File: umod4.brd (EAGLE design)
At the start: 104.9 x 71.1 mm, 94 parts, among them IC3 27C256-FEED-THRU, J1 DMSAT-SF-PEJ, J2 10118194-0001LF, J4 CORTEX_DEBUG-PTH, J5 JST BM08B-SRSS, M1 RPi Pico W, M2 Generic single-sided NEO-8, Q1 C10487/SI2301CDS, Q2 SS8050, U1 74LVC541, U2 74LVC4245, U3 74LVC541, U4 RP2040, U5 W25Q128JVSIQ, U6 74LVC2G04, U7 74LVC2G04, U8 WS2812C-2020, U9 LGS5148, Y1 12MHz

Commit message: Latest changes after github token changed
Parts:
- removed TP2: (no value), SparkFun-Connectors:PAD.03X.05
- added C34: N/S, robins-v7:SMD-0603
- moved JP2 1.78 mm to (34.5, 38.9)
- moved R13 0.76 mm to (58.2, 34.5)
- moved S1 0.51 mm to (63.2, 35.3)
- moved R19 0.25 mm to (8.38, 47.8)
- moved R9 0.25 mm to (8.38, 46.2)
- moved C13 0.25 mm to (24.1, 29.5)
- moved C14 0.25 mm to (24.1, 35.8)
- moved C27 0.25 mm to (24.1, 34.0)
- moved R14 0.25 mm to (24.1, 38.1)
- moved R15 0.25 mm to (24.1, 31.2)
- moved R16 0.25 mm to (24.1, 40.4)
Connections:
- new net SPARE1: M1.31
- net N$16: now also C34.P$2
- net VSYS_1: now also C34.P$1
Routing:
- net +12_US: track 18.3 -> 36.6 mm
- net +3V3: track 336.5 -> 330.9 mm
- net VSYS_1: track 29.7 -> 34.3 mm
- net VIN_MEAS: track 59.4 -> 55.9 mm
- net SPARE1: track 0.00 -> 3.32 mm, vias 0 -> 1
- net SPARE0: track 0.00 -> 3.32 mm, vias 0 -> 1
- net N$16: track 3.98 -> 5.28 mm
- net EP_RUN: track 97.9 -> 96.9 mm
- net N$7: track 36.0 -> 35.1 mm
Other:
- outline, holes or cut-outs redrawn
- board text added: "SP0"
- board text added: "SP1"

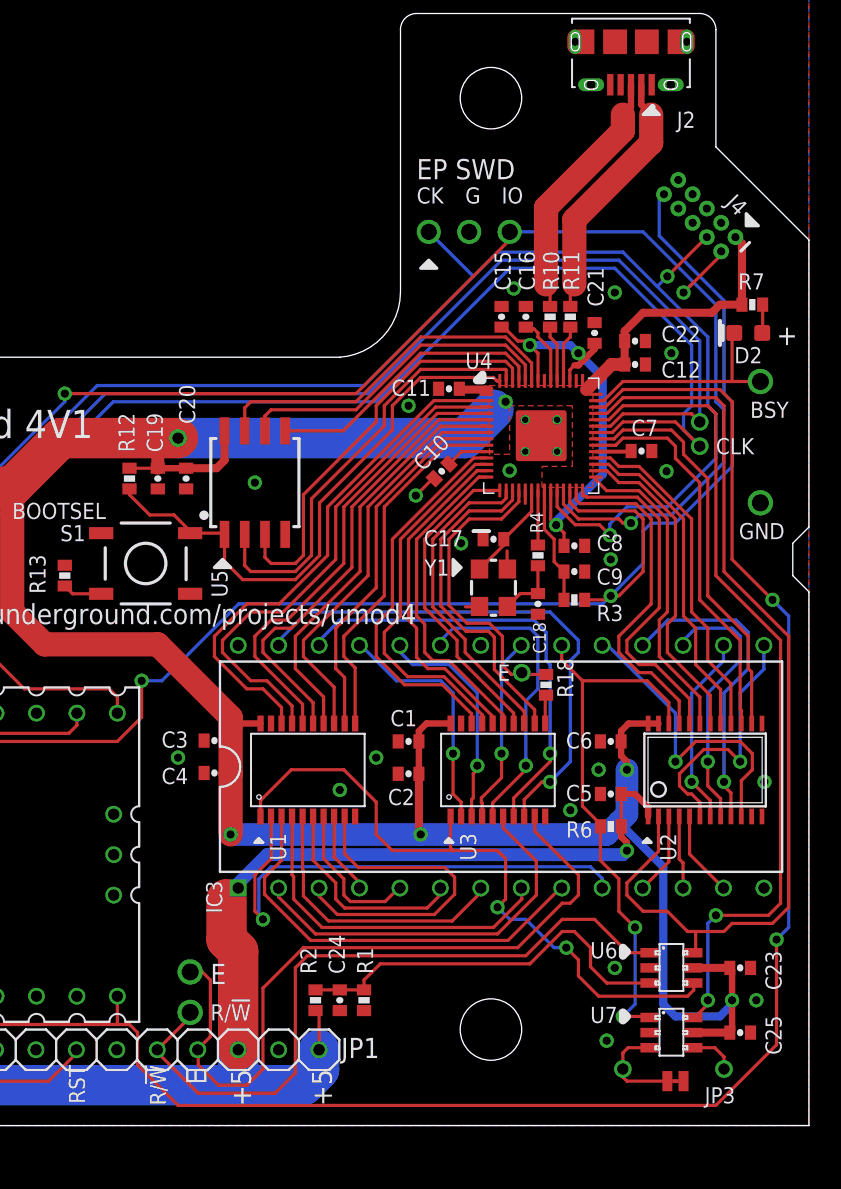
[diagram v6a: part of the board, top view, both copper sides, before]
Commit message: Updated debugger connections for WP, EP
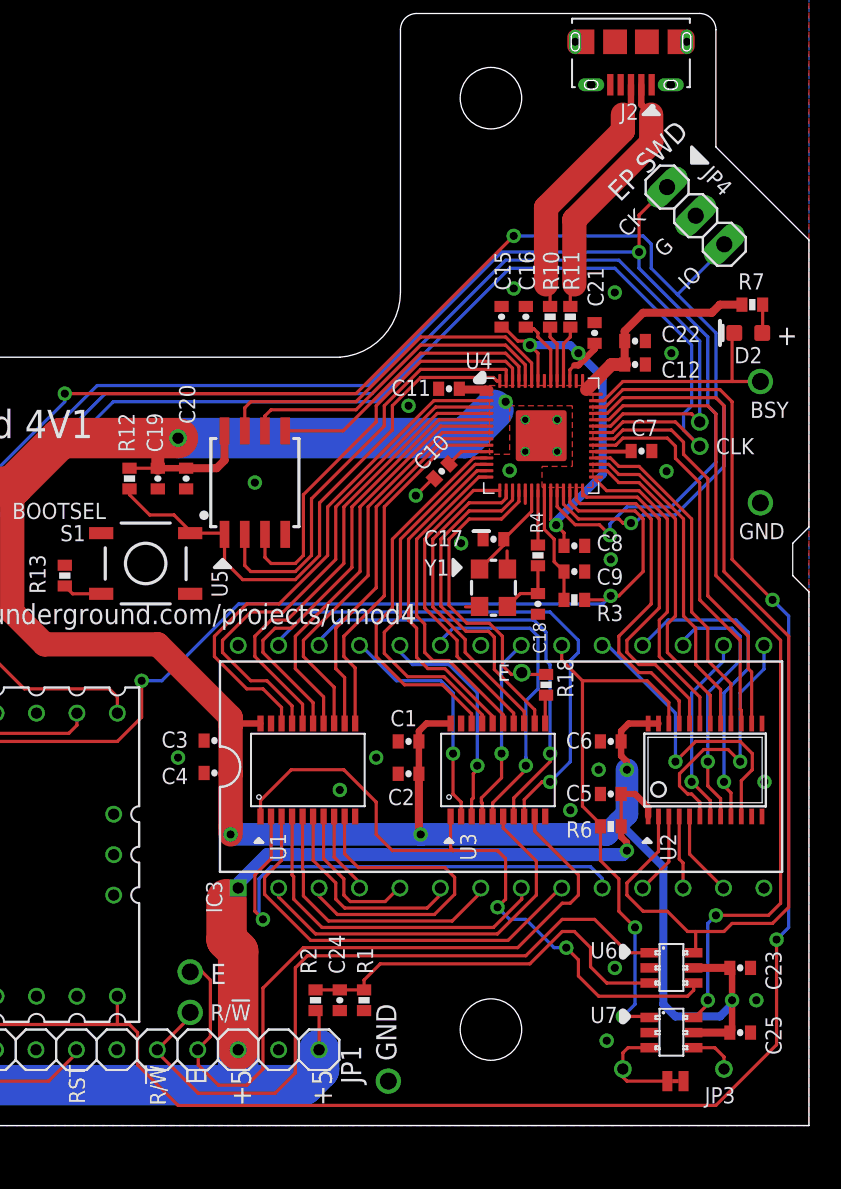
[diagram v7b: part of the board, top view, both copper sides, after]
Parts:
- removed J4: CORTEX_DEBUG-PTH, robins-v7:CON-2X5-1.27MM
- added JP4: (no value), pinhead:1X03
- added TP2: (no value), robins-v7:KEYSTONE-1035
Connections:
- net +3V3: no longer J4.1
- net EP_RUN: no longer J4.10
- net GND: now also JP4.2, TP2.P$1; no longer J4.3, J4.5, J4.9
- net RP_SWCLK: now also JP4.1; no longer J4.4
- net RP_SWD: now also JP4.3; no longer J4.2
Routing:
- net EP_RUN: track 96.9 -> 65.6 mm
- net +3V3: track 330.9 -> 326.5 mm
- net RP_SWCLK: track 137.7 -> 134.9 mm, vias 4 -> 3
- net RP_SWD: track 136.8 -> 136.3 mm, vias 5 -> 4
- net GND: vias 30 -> 29

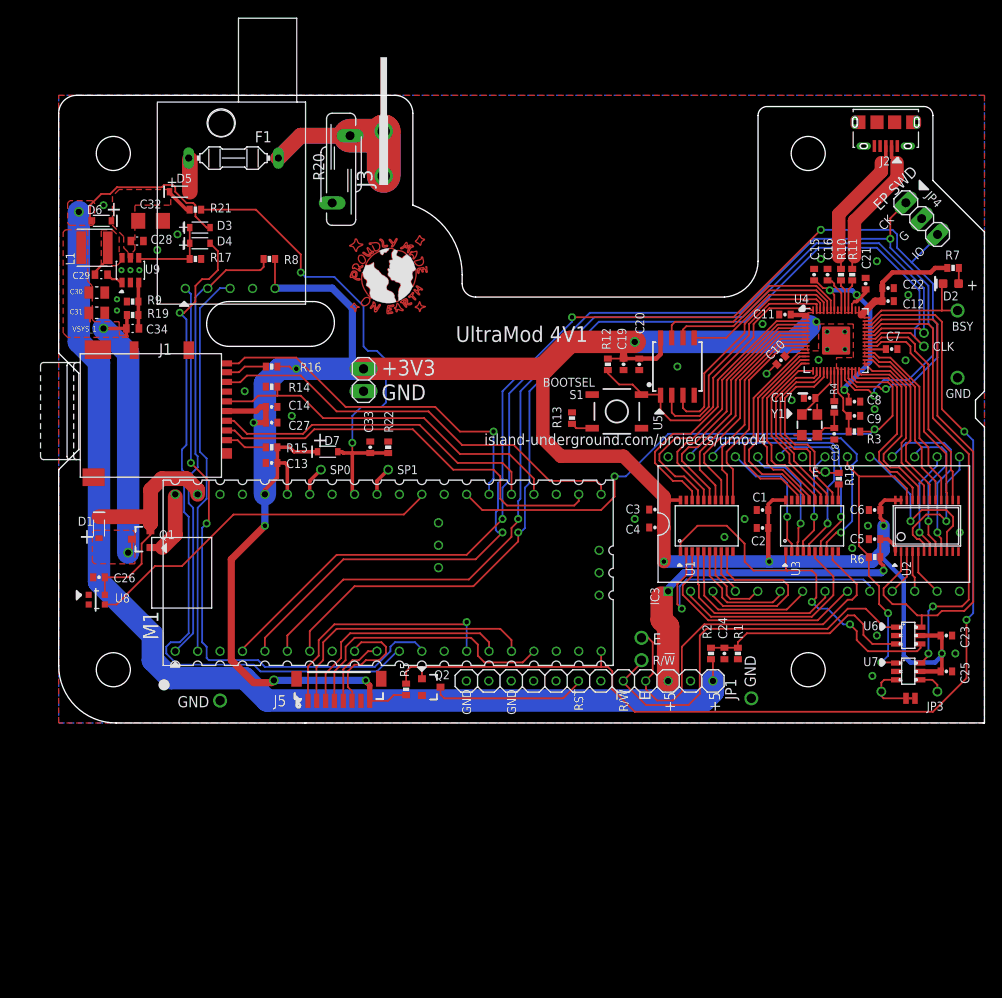
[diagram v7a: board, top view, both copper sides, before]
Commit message: Power Supply Simplification
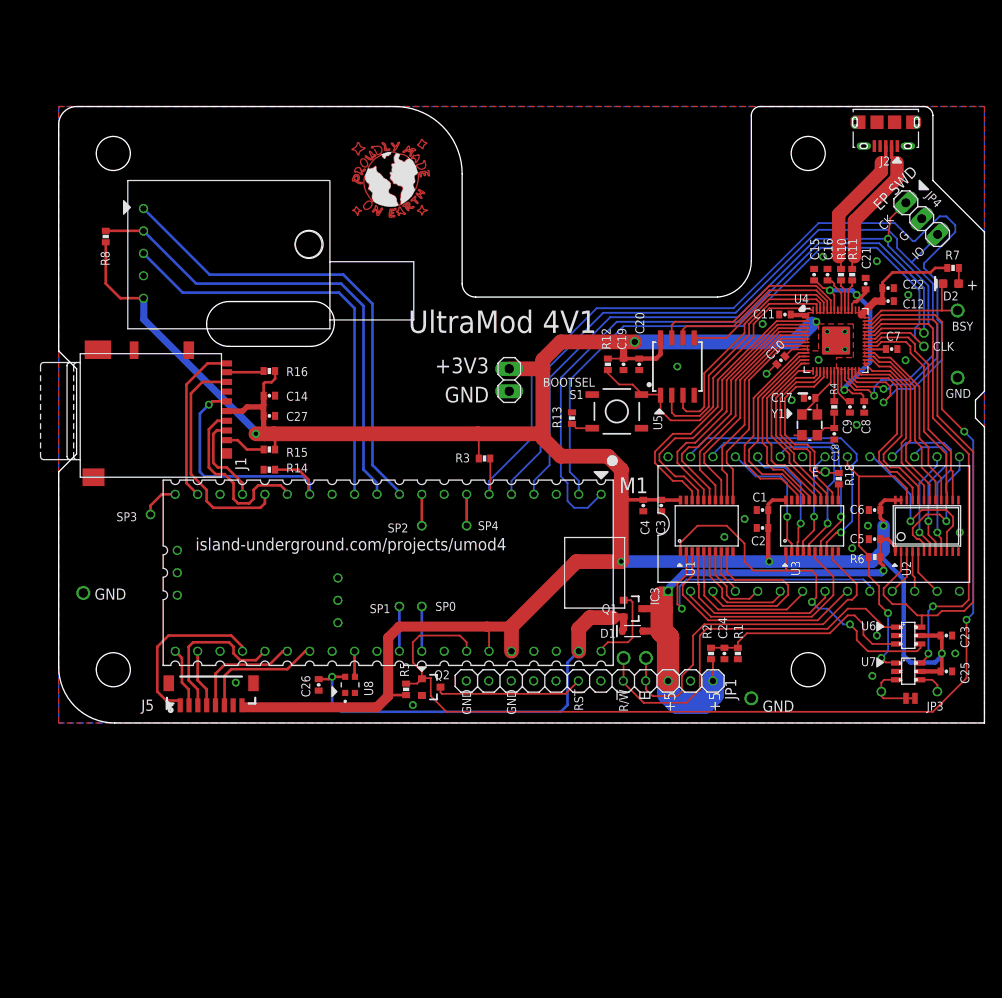
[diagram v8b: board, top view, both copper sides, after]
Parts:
- removed C13, C33: 100n/16V/X7R, SparkFun-03-01-2010:0402-CAP
- removed C28, C29: 100n/50V/X7R, robins-v7:SMD-0603
- removed C30, C31: 10uF/25V/X5R, robins-v7:SMD-0805
- removed C32: 4u7/50V/X7R, SparkFun-Capacitors:1206
- removed C34: N/S, robins-v7:SMD-0603
- removed D3, D4, D5, D6, D7: 1N5819WS, SparkFun-DiscreteSemi:SOD-323
- removed F1: FUSEPICOFUSE, fuse:PICOFUSE
- removed J3: (no value), robins-v7:FASTON-1217756
- removed L1: 22uH, robins-v7:INDUCTOR-CJAING-FHD4020
- removed R17, R19: 10K, SparkFun-03-01-2010:0402-RES
- removed R20: S10K40, varistor:S10K40
- removed R21: 20K, SparkFun-03-01-2010:0402-RES
- removed R22: 5K1, SparkFun-03-01-2010:0402-RES
- removed R9: 56K, SparkFun-03-01-2010:0402-RES
- removed U9: LGS5148, robins-v7:SOT23-6-NT
- moved D1 61.6 mm to (65.0, 10.4), turned to 0 degrees
- moved Q1 56.2 mm to (65.0, 13.0), turned to 270 degrees
- moved R3 42.0 mm to (48.3, 30.0)
- moved U8 30.3 mm to (33.0, 4.32), turned to 270 degrees
- moved C26 27.7 mm to (29.5, 4.32), turned to 270 degrees
- moved M2 21.5 mm to (30.7, 61.5), turned to 180 degrees
- moved TP4 19.7 mm to (2.79, 14.7)
- moved R8 18.7 mm to (5.33, 55.1), turned to 270 degrees
- moved JP2 16.5 mm to (51.1, 38.9)
- moved J5 14.5 mm to (17.3, 3.30)
- moved R14 9.40 mm to (23.9, 28.7)
- moved C4 2.82 mm to (66.2, 24.6), turned to 270 degrees
- moved TP5 2.34 mm to (66.5, 7.37)
- moved TP6 2.05 mm to (64.0, 7.37)
- moved C14 1.30 mm to (23.9, 37.1)
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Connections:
- removed net +12_US: F1.1, J3.1, J3.2, R20.2
- removed net EN: D3.C, D4.C, R17.1, U9.4
- removed net KEEP_ALIVE: D4.A, M1.11
- removed net N$16: C34.P$2, R19.1, R9.2, U9.3
- removed net N$25: D5.A, F1.2
- removed net N$3: C29.P$1, U9.1
- removed net SW: C29.P$2, L1.1, U9.6
- removed net UART0_RX: M1.2, M2.3
- removed net UART0_TX: M1.1, M2.2, R8.1
- removed net VIN: C28.P$1, C32.1, D5.C, D6.C, R21.1, U9.5
- removed net VIN_MEAS: C33.1, D7.A, M1.32, R21.2, R22.1
- removed net VSYS_1: C30.1, C31.1, C34.P$1, D1.A, L1.2, Q1.D, R9.1
- new net PICOW_U0_RX: M1.2, U4.36
- new net PICOW_U0_TX: M1.1, U4.37
- new net SPARE2: M1.9
- new net SPARE3: M1.20
- new net SPARE4: M1.7
- net !CARD: now also M1.19; no longer M1.26
- net !RESET!_HC11_OUT: now also M1.34; no longer M1.20
- net +3V3: no longer C13.1, D7.C
- net +5_ECU: now also D1.A, Q1.D; no longer D3.A, D6.A
- net EP_RUN: now also M1.6; no longer M1.27
- net GND: no longer C13.2, C28.P$2, C30.2, C31.2, C32.2, C33.2, R17.2, R19.2, R20.1, R22.2, U9.2
- net GPS_PPS: now also M1.10; no longer M1.12
- net LCD_BKLT: now also M1.27; no longer M1.9
- net LCD_DC: now also M1.26; no longer M1.10
- net PICOW_U1_RX: now also M1.12, M2.3; no longer M1.7, U4.36
- net PICOW_U1_TX: now also M1.11, M2.2, R8.1; no longer M1.6, U4.37
- net SPARE0: now also M1.32; no longer M1.34
- net SPI0_CS: now also J5.4; no longer J1.CD/DAT3
- net SPI0_MISO: now also J5.2; no longer J1.DAT0
- net SPI0_MOSI: now also J5.3; no longer J1.CMD
- net SPI0_SCK: now also J5.1; no longer J1.CLK, R14.1
- net SPI1_CS: now also J1.CD/DAT3; no longer J5.4
- net SPI1_MISO: now also J1.DAT0; no longer J5.2
- net SPI1_MOSI: now also J1.CMD; no longer J5.3
- net SPI1_SCK: now also J1.CLK, R14.1; no longer J5.1
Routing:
- net +5_ECU: track 189.3 -> 59.5 mm, vias 2 -> 1
- net PICOW_U0_TX: track 0.00 -> 80.7 mm, vias 0 -> 1
- net KEEP_ALIVE: track 80.1 -> 0.00 mm, vias 1 -> 0
- net PICOW_U0_RX: track 0.00 -> 76.4 mm, vias 0 -> 1
- net PICOW_U1_RX: track 115.1 -> 47.6 mm, vias 2 -> 0
- net PICOW_U1_TX: track 115.6 -> 54.7 mm, vias 2 -> 0
- net VIN_MEAS: track 55.9 -> 0.00 mm, vias 2 -> 0
- net UART0_TX: track 51.8 -> 0.00 mm
- net EP_RUN: track 65.6 -> 111.1 mm, vias 2 -> 1
- net UART0_RX: track 44.0 -> 0.00 mm
- net SPI0_MISO: track 48.9 -> 6.76 mm
- net RP_SWCLK: track 134.9 -> 93.2 mm, vias 3 -> 2
- net RP_SWD: track 136.3 -> 95.1 mm, vias 4 -> 1
- net SPI0_CS: track 47.1 -> 6.55 mm
- net WS2812_DI: track 41.2 -> 2.90 mm
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- removed copper zone on layer 1, net +5_ECU
- removed copper zone on layer 1, net SW
- removed copper zone on layer 1, net VIN
- removed copper zone on layer 1, net VSYS_1
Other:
- board size 104.9 x 71.1 mm -> 104.9 x 69.8 mm
- board text added: "SP2"
- board text added: "SP3"
- board text added: "SP4"
- board text removed: "VSYS_1"
